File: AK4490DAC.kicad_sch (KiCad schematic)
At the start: 60 parts, among them IC1 LP5907MFX-3.3/NOPB, IC2 LP5907MFX-3.3/NOPB, IC3 LP5907MFX-3.3/NOPB, IC4 TPS7A2050PDBVR, IC5 MUSES8920, IC6 MUSES8920, IC7 MUSES8920, IC8 TPS7A2050PDBVR, IC9 AMS1117, J1 JST_XA_B02B-XASK-1, J2 USB_B_Micro, J3 SPDIF_IN, T1 DA103C, U1 SN74LS06NSR, U2 PCM2704CDBR, U3 TCM809TENB713, U4 TCM809TENB713, U5 AK4118, U6 AK4490, U7 MCWI03-12D15, Y1 11.2896MHz, Y2 12MHz

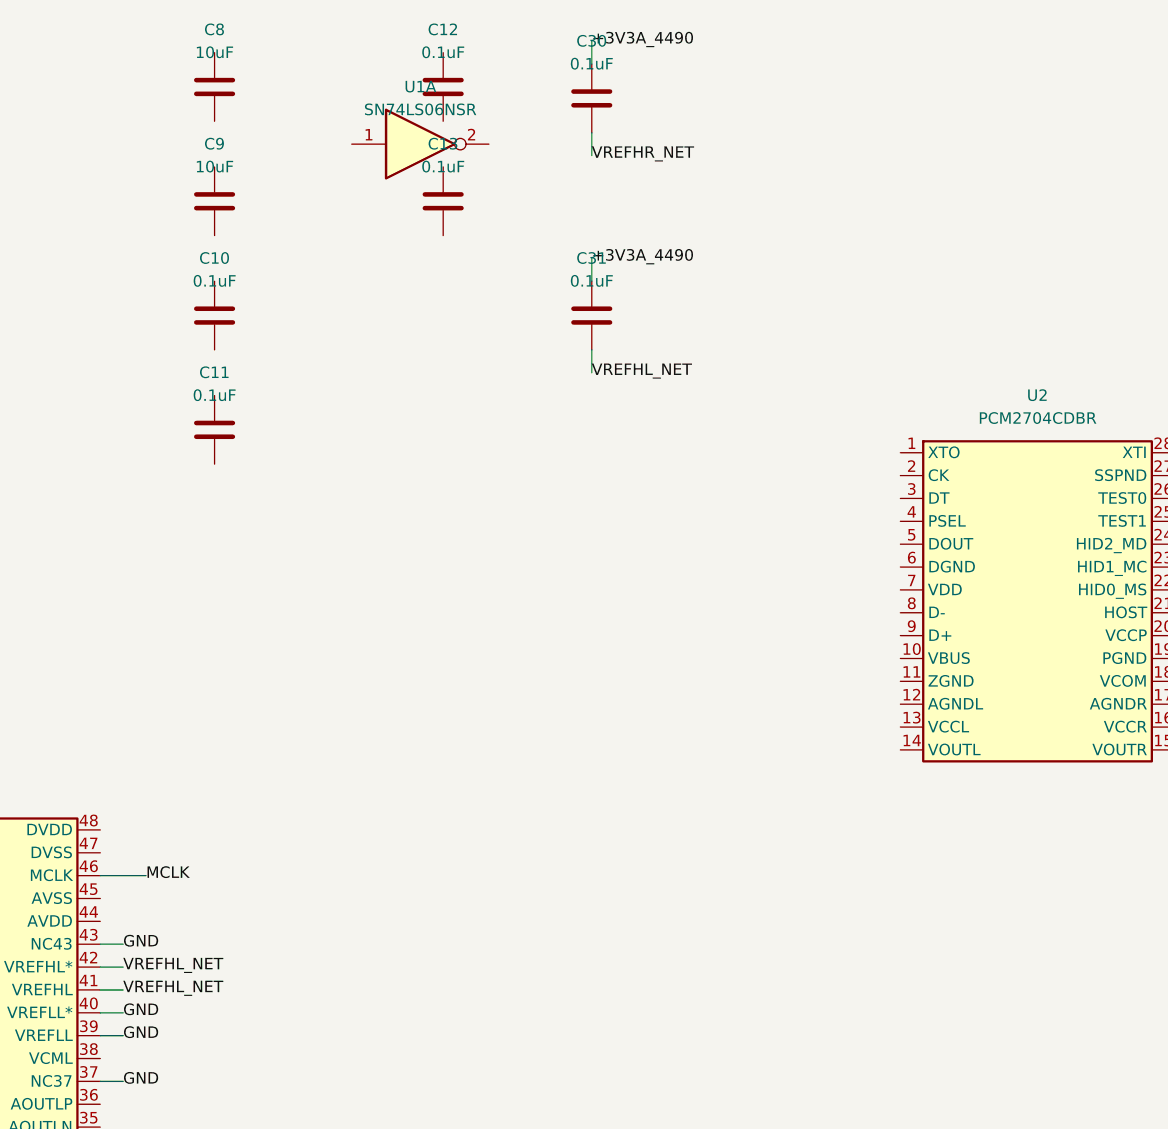
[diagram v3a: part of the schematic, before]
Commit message: Place Fig.40 differential-to-single-ended output filter components
Switched from the Fig.41 topology discussed earlier to Fig.40 (single
op-amp per channel): the exact per-component node connections in
Fig.41 could not be read with full confidence from the datasheet scan,
and getting a differential audio output stage wrong is exactly the
class of mistake this session has already made once (the earlier
current-output/I-V assumption). Fig.40's values are all clearly
legible and its frequency response is independently documented
(Table 30), so it's the safer choice to implement correctly.

Places (unwired) the classic 4-resistor difference-amplifier + 2-pole
filter per channel, using AKM's exact Fig.40 values:
  Ra1, Ra2 = 1.5k (AOUTxN / AOUTxP input resistors)
  Cdiff = 2.2nF (cross-coupled between the two input nodes, forms the
    differential-mode pole while preserving common-mode rejection)
  Rb1, Rb2 = 390R (series into the op-amp's -/+ inputs)
  Rf = 1.5k, Cf = 1nF (feedback, inverting input to output)
  Rg = 1.5k, Cg = 1nF (non-inverting input to GND, mirrors Rf/Cf for
    balanced CMRR -- required for a proper difference amplifier)
  + output DC-block coupling cap (1uF) and line-out connector per ch

Only 2 of the 6 available MUSES8920 op-amp units are used (IC5 unit 1
for L, IC6 unit 1 for R) -- the other 4 units (IC5 unit 2, IC6 unit 2,
IC7 units 1/2) stay placed and power-wired but otherwise spare for
future use.

Verified via kicad-cli sch erc: 324 violations, no new violation
categories, no crash.

Still pending: wiring this network to AK4490's AOUTxP/AOUTxN pins, the
op-amp inputs/output, and GND.

Co-Authored-By: Claude Sonnet 5 <noreply@anthropic.com>
Claude-Session: https://claude.ai/code/session_01UHxU1bYnUhoAmCyc4Koj96
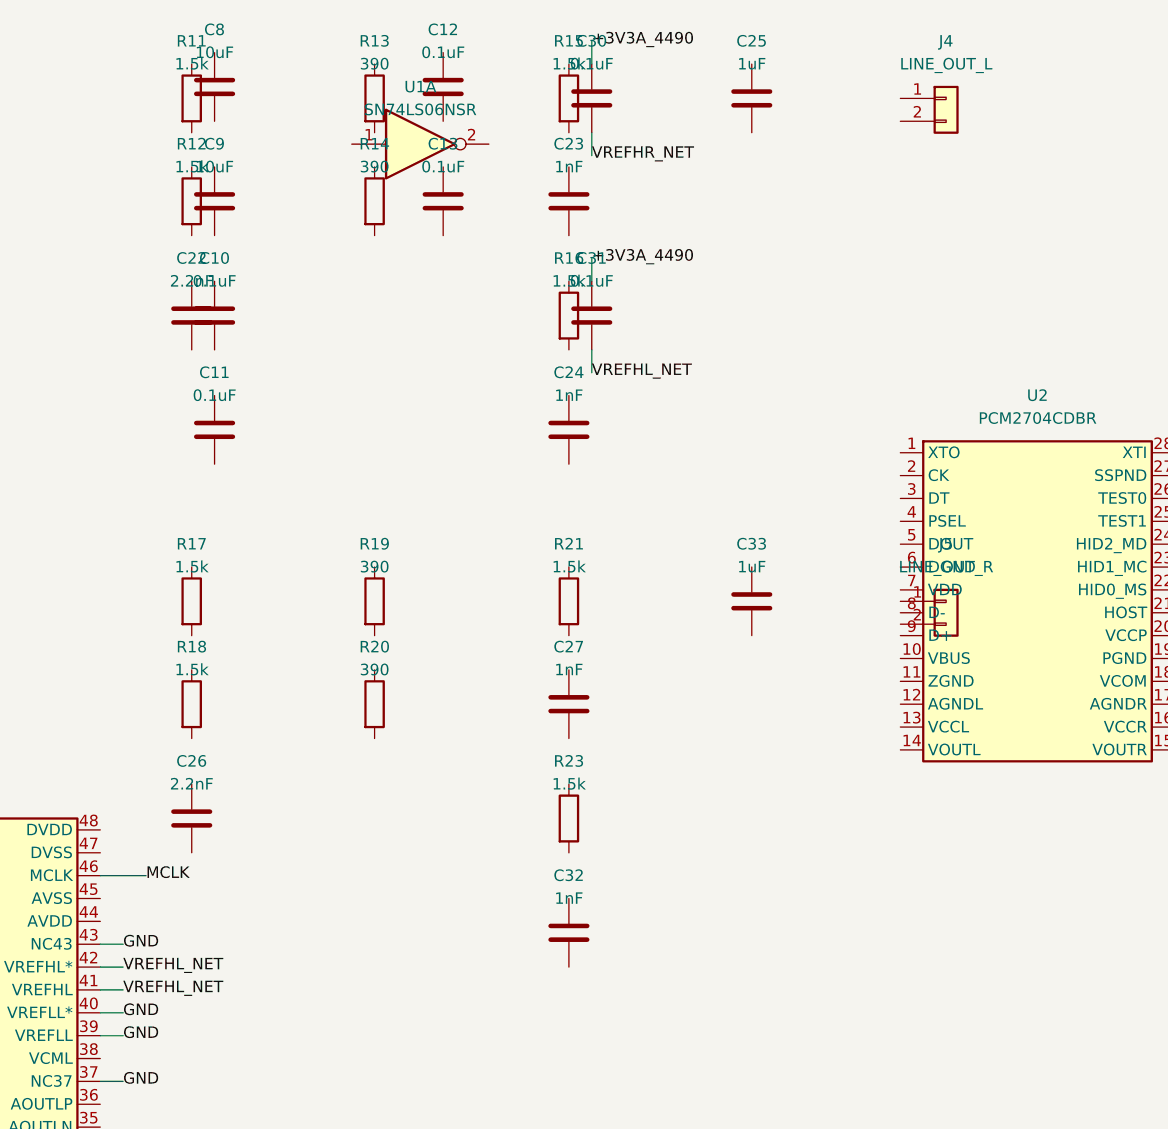
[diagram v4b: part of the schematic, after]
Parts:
- added C22, C26: 2.2nF, Capacitor_SMD:C_0603_1608Metric, symbol Device:C
- added C23, C24, C27, C32: 1nF, Capacitor_SMD:C_0603_1608Metric, symbol Device:C
- added C25, C33: 1uF, Capacitor_SMD:C_0603_1608Metric, symbol Device:C
- added J4: LINE_OUT_L, symbol Connector_Generic:Conn_01x02
- added J5: LINE_OUT_R, symbol Connector_Generic:Conn_01x02
- added R11, R12, R15, R16, R17, R18, R21, R23: 1.5k, Resistor_SMD:R_0603_1608Metric, symbol Device:R
- added R13, R14, R19, R20: 390, Resistor_SMD:R_0603_1608Metric, symbol Device:R

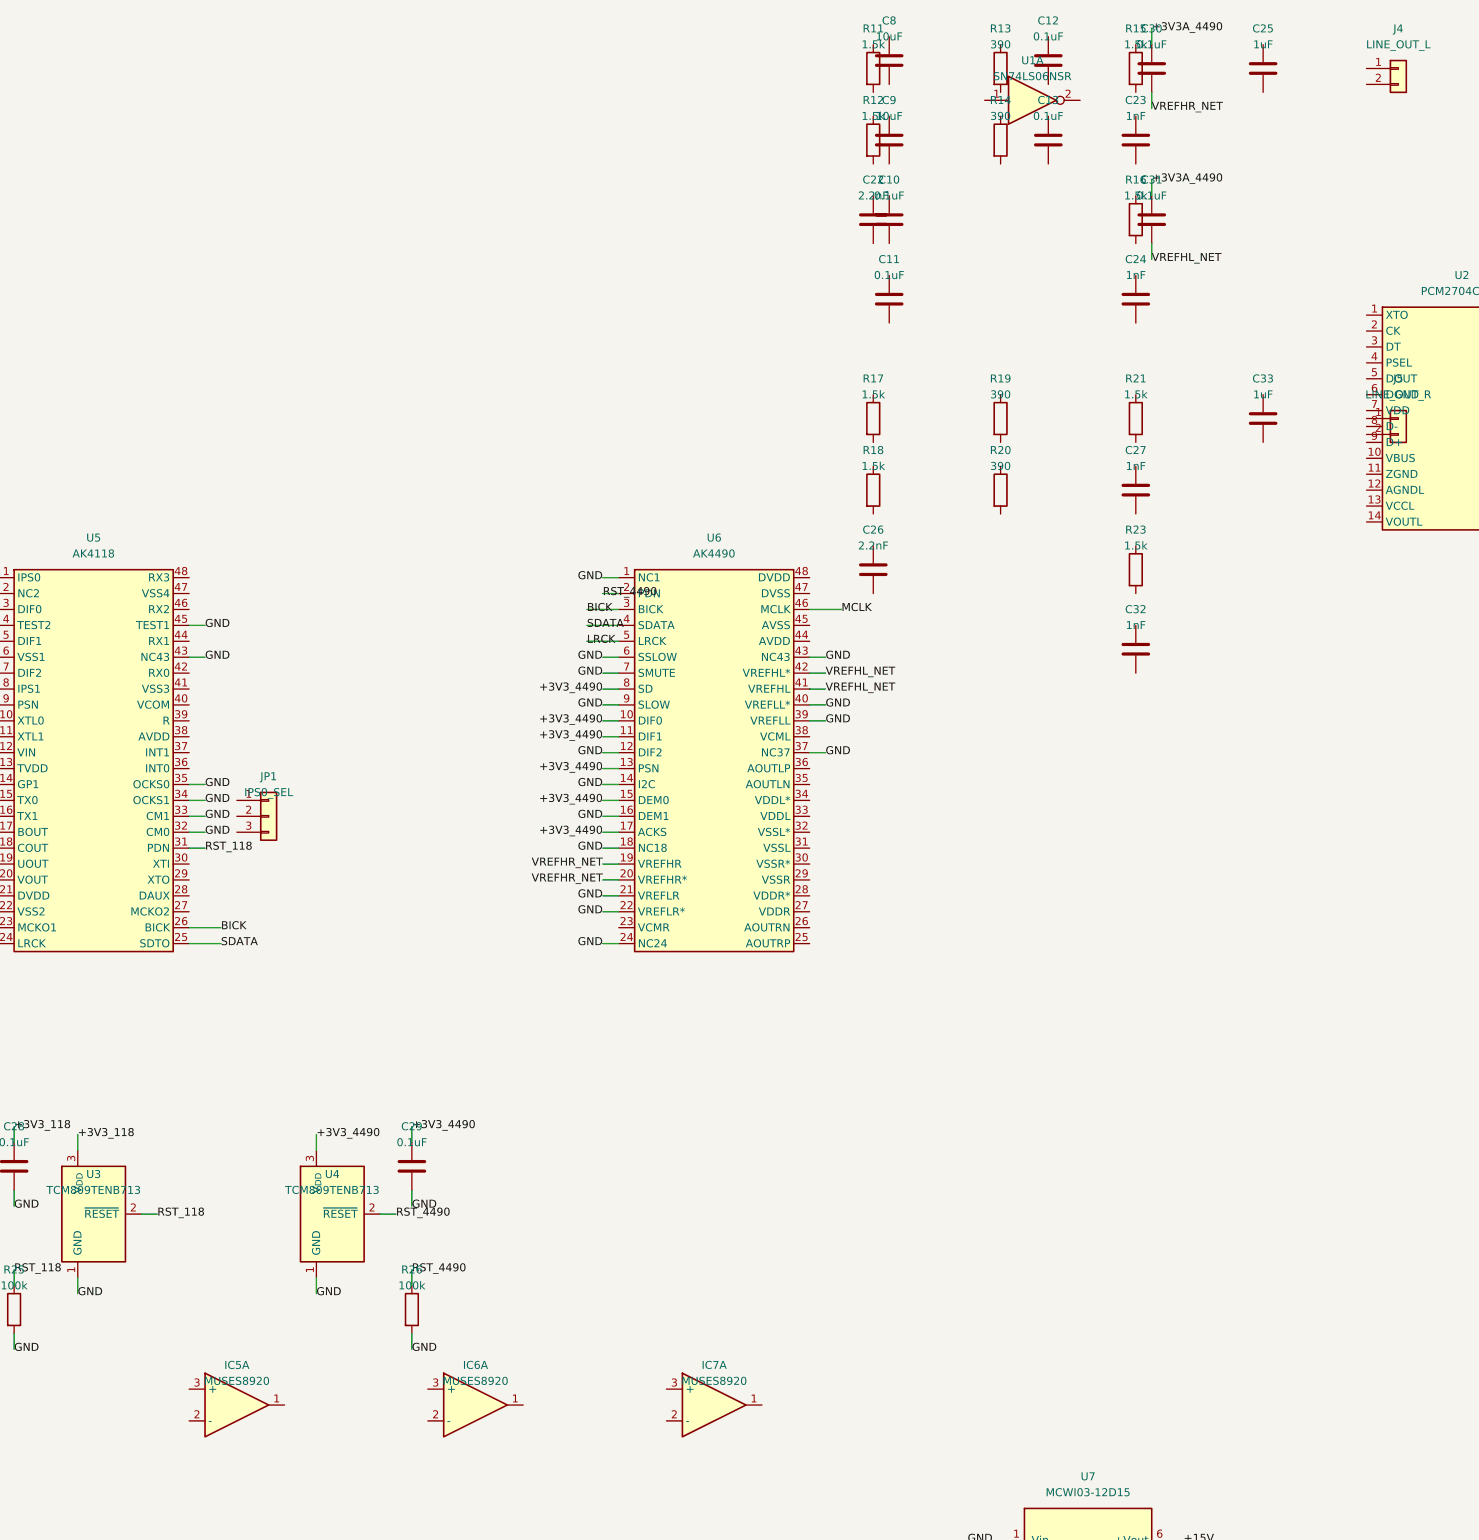
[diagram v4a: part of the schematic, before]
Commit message: Wire the Fig.40 output filter network to AK4490 and the op-amps
Connects the components placed in the previous commit into the actual
difference-amplifier + 2-pole LPF per channel, using the project's
established stub-wire + label style:

  AOUTxN/AOUTxP -> Ra1/Ra2 (1.5k) -> {NODE1,NODE2} -> Cdiff (2.2nF
  cross-coupled) -> Rb1/Rb2 (390R) -> op-amp -/+ inputs
  op-amp output <-> Rf/Cf (1.5k || 1nF) feedback to inverting input
  non-inverting input <-> Rg/Cg (1.5k || 1nF) to GND (mirrors the
  feedback impedance for balanced CMRR, per the difference-amp
  topology)
  op-amp output -> Cout (1uF) -> line-out connector

L channel uses IC5 unit 1, R channel uses IC6 unit 1 (matches the
Fig.40-topology decision from the previous two commits).

Bug found and fixed before verifying: with the usual 2.54mm wire-stub
length, several of these nodes are spaced exactly 12.7mm apart (e.g.
R12/C22), so a stub from one component's pin and a stub from the next
component's pin landed on the exact same coordinate -- KiCad merged
those into one net despite carrying two different labels. This
collapsed L_NODE1/L_NODE2 together and L_OUT/L_NONINV together, which
cascaded (via the now-shorted feedback path) into shorting AOUTLP_SIG,
AOUTRP_SIG, both channels' op-amp outputs, and GND all onto one net --
caught via the resulting pin_to_pin and multiple_net_names ERC
violations before this was ever exported or fabricated. Fixed by
shortening the stub length to 1.27mm (still grid-aligned) so adjacent
component stubs no longer reach far enough to coincide, and added a
coordinate-collision check to the generator script that would have
caught this immediately had it been there from the start.

Verified via kicad-cli sch erc: 265 violations, lib_symbol_mismatch=10
(unchanged from the previous commit's explained baseline), no new
violation categories, no crash.

This completes the output stage rework (I/V-assumption removal ->
isolated +-15V supply -> Fig.40 topology placement -> wiring). Op-amp
un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
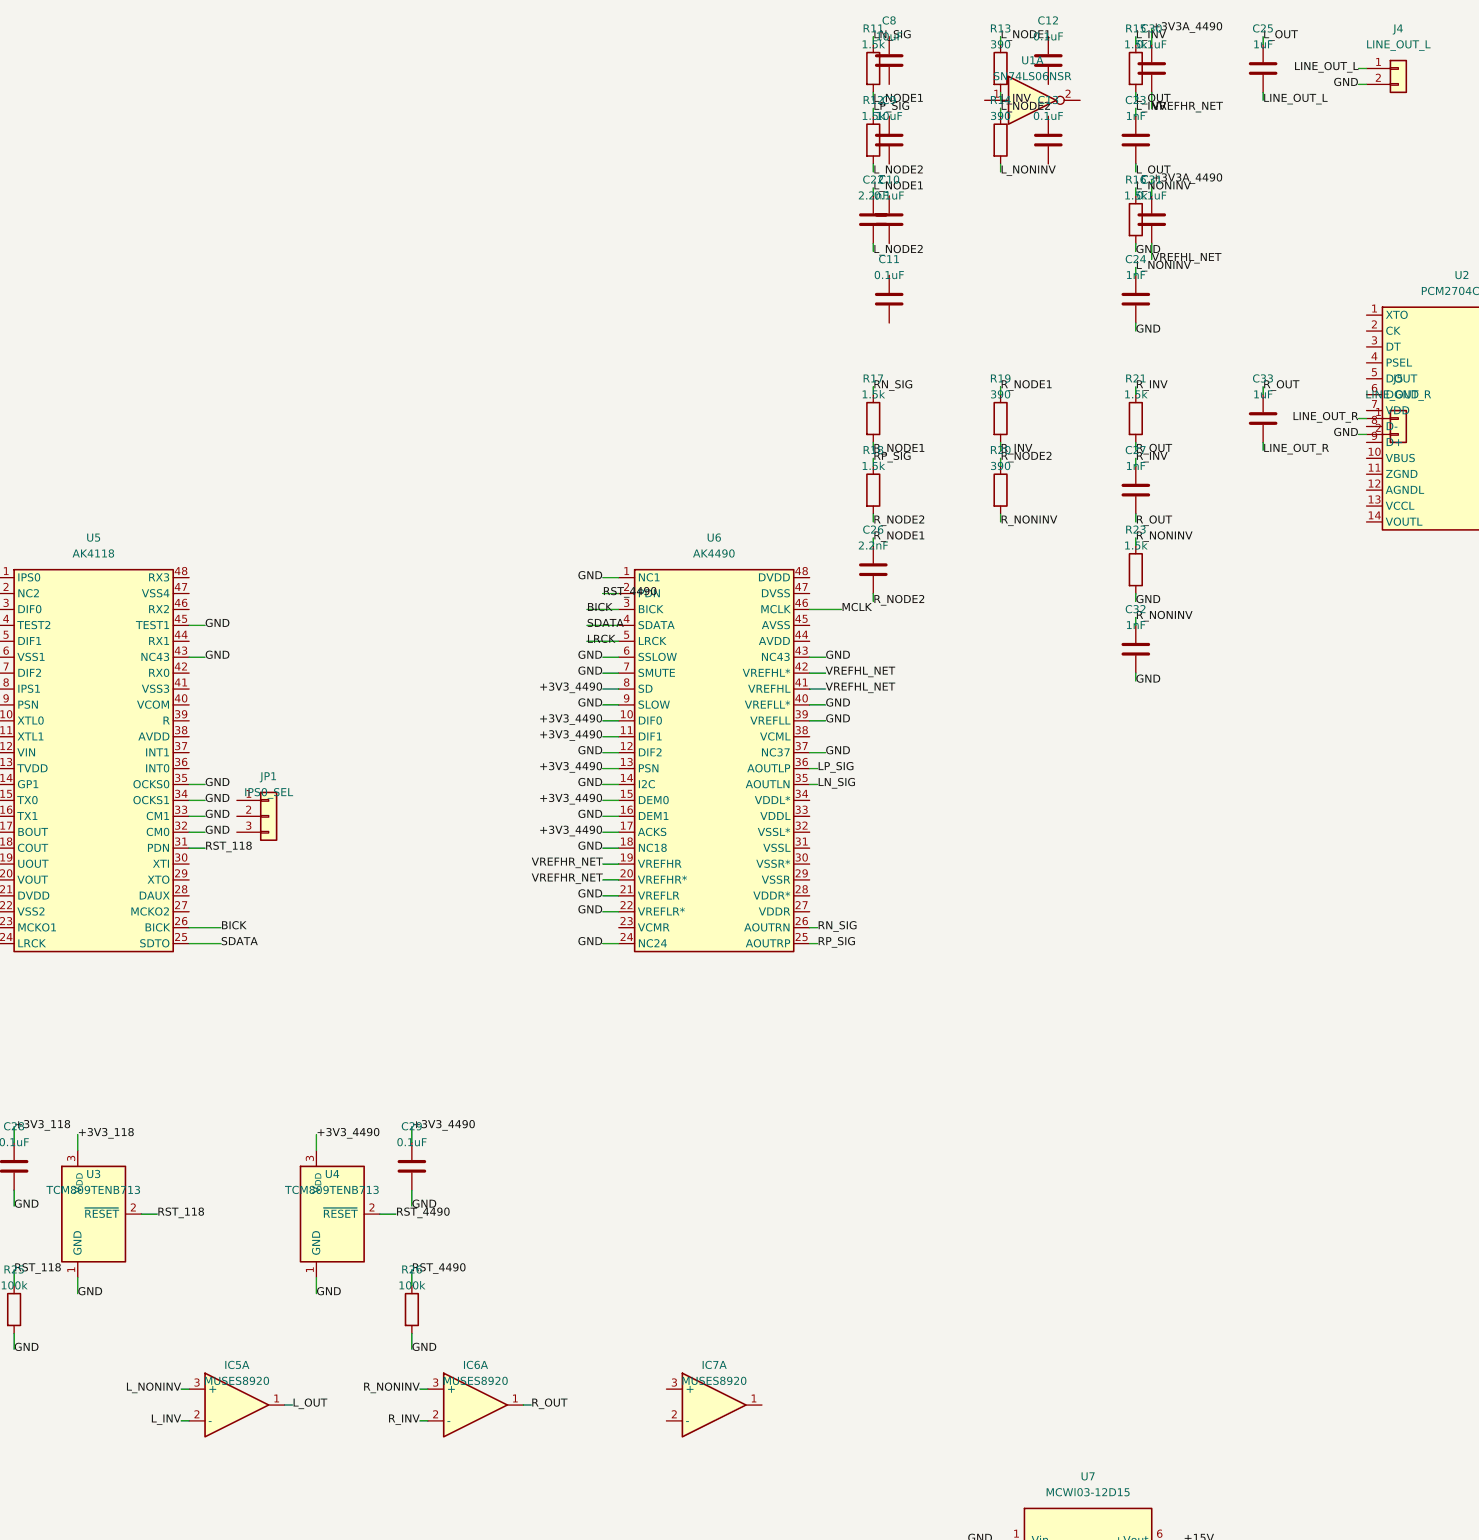
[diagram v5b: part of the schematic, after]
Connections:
- net GND: now also C24.2, C32.2, J4.2 (Pin_2), J5.2 (Pin_2), R16.2, R23.2
- net LINE_OUT_R: now reaches J5.1 (Pin_1)
- net LINE_OUT_R: now also C33.2
- net R_NODE2: now reaches R20.1
- net R_NODE2: now also C26.2, R18.2
- net R_NONINV: now reaches R20.2
- net R_NONINV: now also C32.1, IC6.3 (+), R23.1
- net L_NONINV: now reaches R16.1
- net L_NONINV: now also C24.1, IC5.3 (+), R14.2
- net L_NODE1: now reaches R13.1
- net L_NODE1: now also C22.1, R11.2
- net L_INV: now reaches R13.2
- net L_INV: now also C23.1, IC5.2 (-), R15.1
- net L_NODE2: now reaches C22.2
- net L_NODE2: now also R12.2, R14.1
- net RP_SIG: now reaches R18.1
- net RP_SIG: now also U6.25 (AOUTRP)
- net LINE_OUT_L: now reaches J4.1 (Pin_1)
- net LINE_OUT_L: now also C25.2
- net L_OUT: now reaches IC5.1
- net L_OUT: now also C23.2, C25.1, R15.2
- net R_OUT: now reaches C33.1
- net R_OUT: now also C27.2, IC6.1, R21.2
- net R_NODE1: now reaches C26.1
- net R_NODE1: now also R17.2, R19.1
- net R_INV: now reaches IC6.2 (-)
- net R_INV: now also C27.1, R19.2, R21.1
- net LN_SIG: now reaches R11.1
- net LN_SIG: now also U6.35 (AOUTLN)
- net RN_SIG: now reaches U6.26 (AOUTRN)
- net RN_SIG: now also R17.1
- net LP_SIG: now reaches U6.36 (AOUTLP)
- net LP_SIG: now also R12.1
